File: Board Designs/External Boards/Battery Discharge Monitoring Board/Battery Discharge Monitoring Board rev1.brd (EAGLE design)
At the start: 170.2 x 120.3 mm, 71 parts

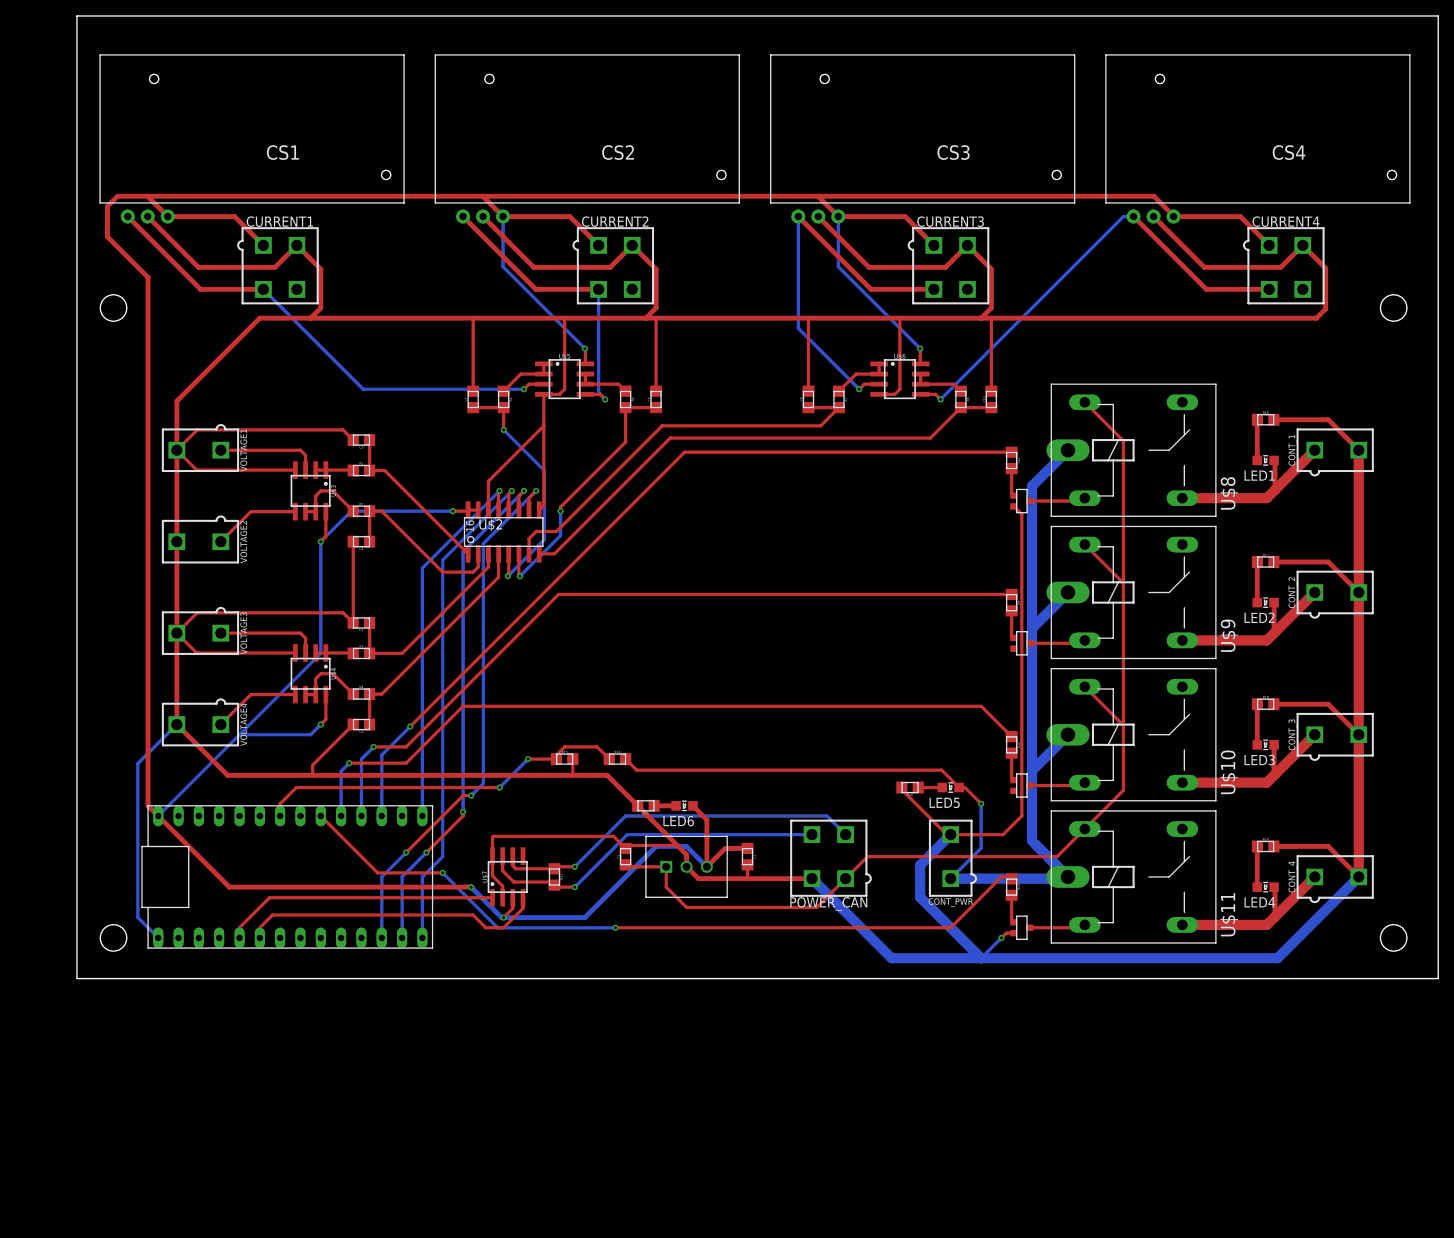
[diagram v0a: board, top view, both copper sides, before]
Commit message: Add 10k resistors to current sensors, fix DRC errors, small silkscreen tweaks for mfg
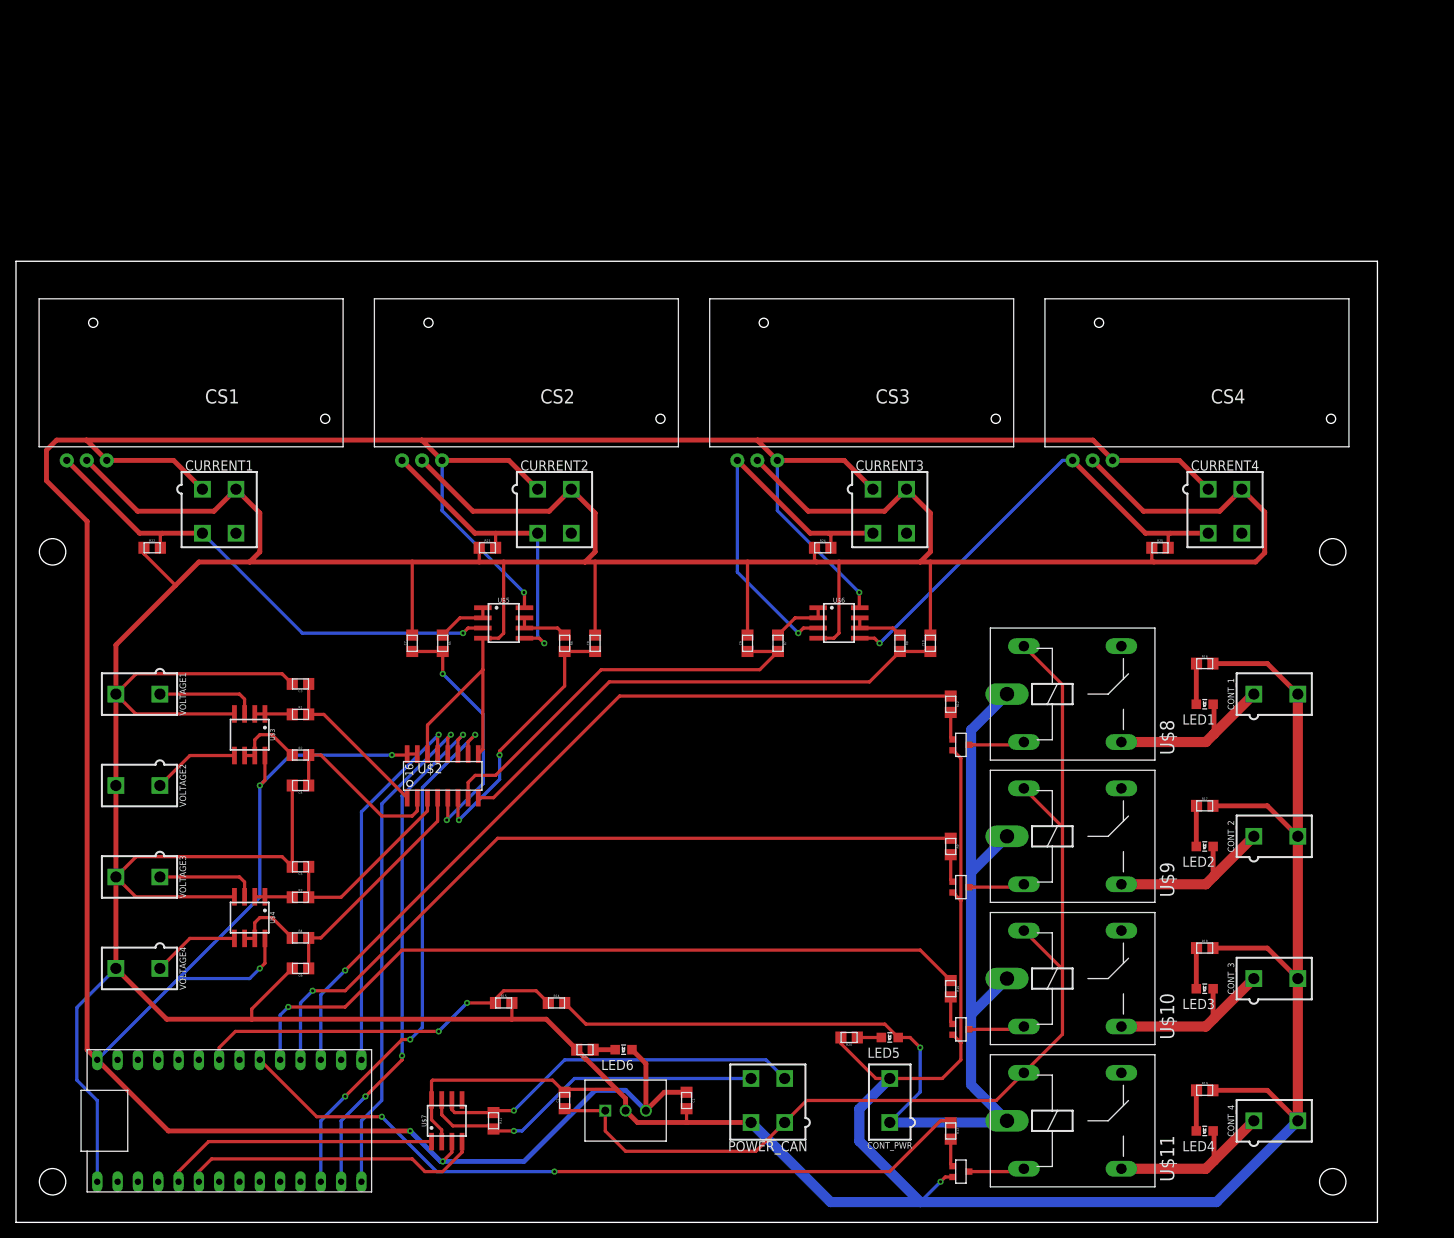
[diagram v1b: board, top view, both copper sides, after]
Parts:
- added R22, R23, R24, R25: 10k, HyTechDevices:0805
- moved LED5 32.2 mm to (109.2, 23.1)
- moved R20 32.2 mm to (104.1, 23.1)
- moved C10 31.4 mm to (114.3, 72.4)
- moved C3 31.4 mm to (35.6, 67.3)
- moved C4 31.4 mm to (35.6, 54.6)
- moved C5 31.4 mm to (35.6, 44.5)
- moved C7 31.4 mm to (49.5, 72.4)
- moved C8 31.4 mm to (72.4, 72.4)
- moved C9 31.4 mm to (91.4, 72.4)
- moved CS1 31.4 mm to (6.35, 95.2)
- moved CS2 31.4 mm to (48.3, 95.2)
- moved CS3 31.4 mm to (90.2, 95.2)
- moved LED1 31.4 mm to (148.6, 64.8)
- moved Q1 31.4 mm to (118.1, 59.7)
- moved Q2 31.4 mm to (118.1, 41.9)
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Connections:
- net CUR_SENSE_1: now also R22.2
- net CUR_SENSE_2: now also R23.2
- net CUR_SENSE_3: now also R24.2
- net CUR_SENSE_4: now also R25.2
- net GND: now also R22.1, R23.1, R24.1, R25.1
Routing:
- net GND: track 921.2 -> 936.4 mm
- net CUR_SENSE_3: track 48.2 -> 50.1 mm
- net CUR_SENSE_4: track 57.1 -> 59.0 mm
- net CUR_SENSE_1: track 61.2 -> 63.1 mm
- net CUR_SENSE_2: track 37.6 -> 39.4 mm
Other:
- board size 170.2 x 120.3 mm -> 170.2 x 120.1 mm
- board text added: "Install either current sensor or connector, not both (4x)"
- board text removed: "Install either current sensor or connector, not both"

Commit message: Updated resistor values for BJTs
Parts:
- R10, R12, R13, R9: value 2.2k -> 1k
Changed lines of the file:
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@@
 <drawing>
 <settings>
-<setting alwaysvectorfont="no"/>
+<setting alwaysvectorfont="yes"/>
 <setting verticaltext="up"/>
 </settings>
-<grid distance="20" unitdist="mil" unit="mil" style="lines" multiple="1" display="yes" altdistance="5" altunitdist="mil" altunit="mil"/>
+<grid distance="50" unitdist="mil" unit="mil" style="lines" multiple="1" display="yes" altdistance="5" altunitdist="mil" altunit="mil"/>
 <layers>
 <layer number="1" name="Top" color="4" fill="1" visible="yes" active="yes"/>
@@
 <attribute name="VALUE" x="35.56" y="62.7888" size="0.3048" layer="27" align="top-center"/>
 </element>
-<element name="R10" library="HyTechDevices" package="0805" value="2.2k" x="116.84" y="29.21" smashed="yes" rot="R270">
+<element name="R10" library="HyTechDevices" package="0805" value="1k" x="116.84" y="29.21" smashed="yes" rot="R270">
 <attribute name="NAME" x="117.5639" y="29.21" size="0.3048" layer="25" rot="R270" align="bottom-center"/>
 <attribute name="VALUE" x="116.1288" y="29.21" size="0.3048" layer="27" rot="R270" align="top-center"/>
@@
 <attribute name="VALUE" x="58.9788" y="12.7" size="0.3048" layer="27" rot="R270" align="top-center"/>
 </element>
-<element name="R12" library="HyTechDevices" package="0805" value="2.2k" x="116.84" y="64.77" smashed="yes" rot="R270">
+<element name="R12" library="HyTechDevices" package="0805" value="1k" x="116.84" y="64.77" smashed="yes" rot="R270">
 <attribute name="NAME" x="117.5639" y="64.77" size="0.3048" layer="25" rot="R270" align="bottom-center"/>
 <attribute name="VALUE" x="116.1288" y="64.77" size="0.3048" layer="27" rot="R270" align="top-center"/>
 </element>
-<element name="R13" library="HyTechDevices" package="0805" value="2.2k" x="116.84" y="11.43" smashed="yes" rot="R270">
+<element name="R13" library="HyTechDevices" package="0805" value="1k" x="116.84" y="11.43" smashed="yes" rot="R270">
 <attribute name="NAME" x="117.5639" y="11.43" size="0.3048" layer="25" rot="R270" align="bottom-center"/>
 <attribute name="VALUE" x="116.1288" y="11.43" size="0.3048" layer="27" rot="R270" align="top-center"/>
@@
 <attribute name="VALUE" x="109.7788" y="72.39" size="0.3048" layer="27" rot="R270" align="top-center"/>
 </element>
-<element name="R9" library="HyTechDevices" package="0805" value="2.2k" x="116.84" y="46.99" smashed="yes" rot="R270">
+<element name="R9" library="HyTechDevices" package="0805" value="1k" x="116.84" y="46.99" smashed="yes" rot="R270">
 <attribute name="NAME" x="117.5639" y="46.99" size="0.3048" layer="25" rot="R270" align="bottom-center"/>
 <attribute name="VALUE" x="116.1288" y="46.99" size="0.3048" layer="27" rot="R270" align="top-center"/>

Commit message: Added value for BJTs indicating part number
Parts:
- Q1, Q2, Q3, Q4: value (none) -> LMMBT3904LT3G
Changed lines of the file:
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@@
 <attribute name="VALUE" x="93.98" y="21.59" size="1.27" layer="27" align="bottom-center"/>
 </element>
-<element name="Q1" library="HyTechDevices" package="SOT23" value="" x="118.11" y="59.69" smashed="yes" rot="R270"/>
-<element name="Q2" library="HyTechDevices" package="SOT23" value="" x="118.11" y="41.91" smashed="yes" rot="R270"/>
-<element name="Q3" library="HyTechDevices" package="SOT23" value="" x="118.11" y="24.13" smashed="yes" rot="R270"/>
-<element name="Q4" library="HyTechDevices" package="SOT23" value="" x="118.11" y="6.35" smashed="yes" rot="R270"/>
+<element name="Q1" library="HyTechDevices" package="SOT23" value="LMMBT3904LT3G" x="118.11" y="59.69" smashed="yes" rot="R270"/>
+<element name="Q2" library="HyTechDevices" package="SOT23" value="LMMBT3904LT3G" x="118.11" y="41.91" smashed="yes" rot="R270"/>
+<element name="Q3" library="HyTechDevices" package="SOT23" value="LMMBT3904LT3G" x="118.11" y="24.13" smashed="yes" rot="R270"/>
+<element name="Q4" library="HyTechDevices" package="SOT23" value="LMMBT3904LT3G" x="118.11" y="6.35" smashed="yes" rot="R270"/>
 <element name="R1" library="HyTechDevices" package="0805" value="" x="35.56" y="63.5" smashed="yes">
 <attribute name="NAME" x="35.56" y="64.2239" size="0.3048" layer="25" align="bottom-center"/>
